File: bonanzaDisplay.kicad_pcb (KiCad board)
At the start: 6 copper layers, 76 x 101 mm, 63 parts, among them J1 OLED-1.31-SSD1322, J15 SWD, J5 Conn_01x10, J6 USB_C_Receptacle_USB2.0, SW1 TS-1088-AR02016, SW2 TS-1088-AR02016, SW4 7*7*5-6P WX, U1 RP2354A, U10 TPS82130, U2 XC6206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

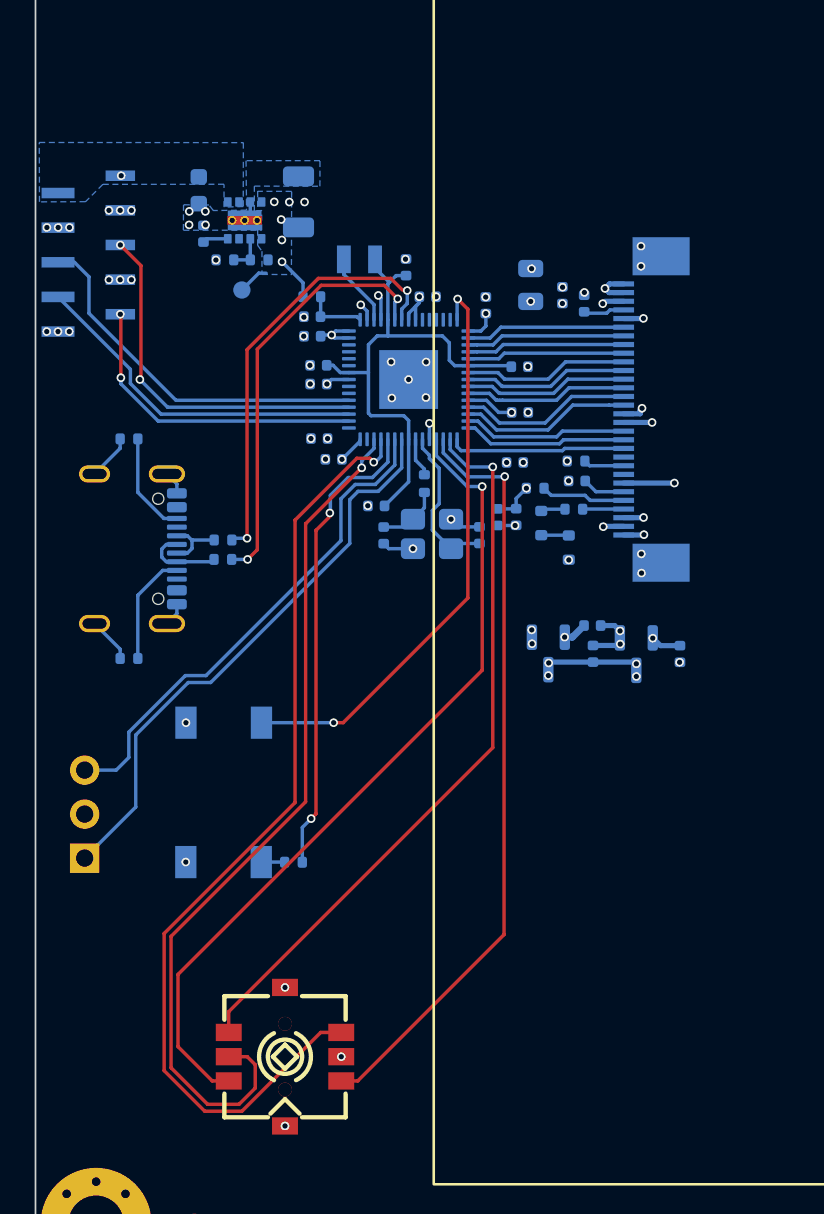
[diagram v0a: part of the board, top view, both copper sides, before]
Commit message: routing cleanup
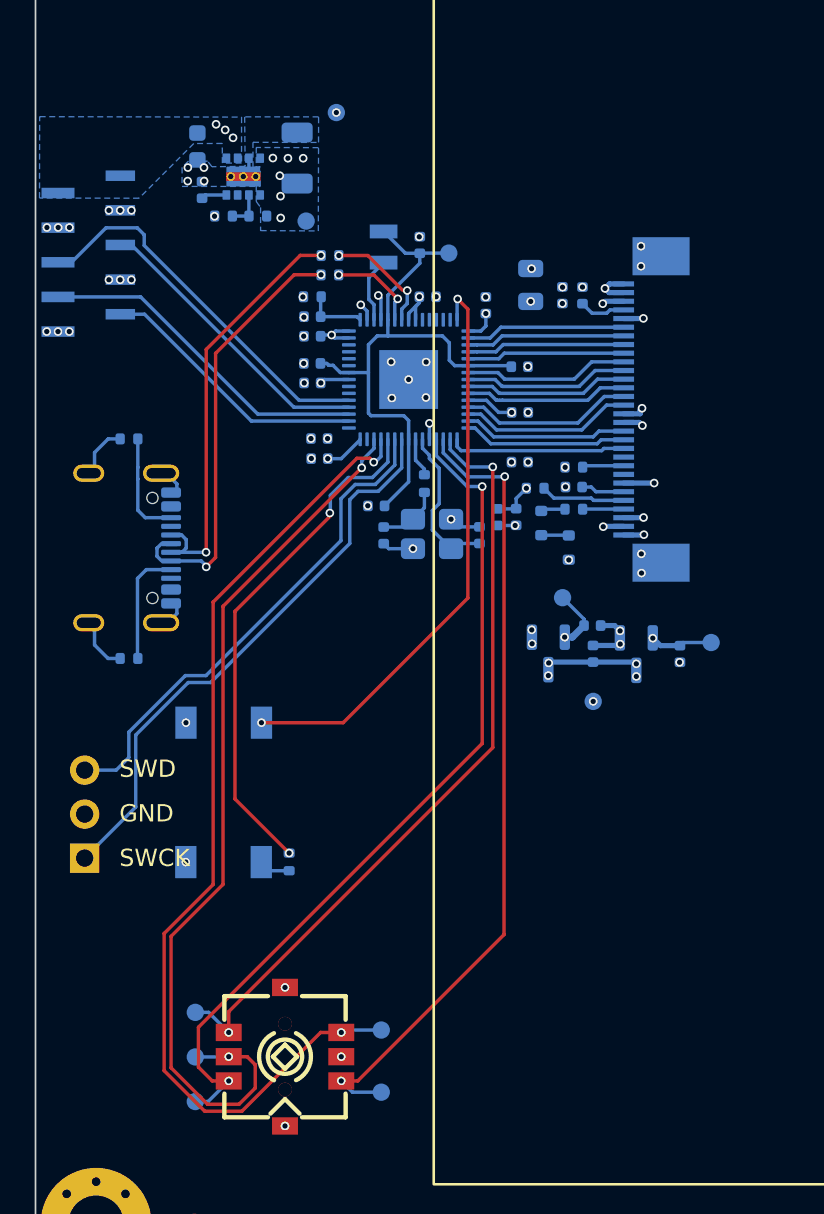
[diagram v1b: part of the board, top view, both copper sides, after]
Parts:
- added TP10: SW_D, bonanzaDisplay:TestPoint_Pad_D1.0mm, B.Cu at (120.0, 125.3)
- added TP11: SW_B, bonanzaDisplay:TestPoint_Pad_D1.0mm, B.Cu at (120.0, 128.9)
- added TP12: SW_A, bonanzaDisplay:TestPoint_Pad_D1.0mm, B.Cu at (109.2, 124.3)
- added TP13: SW_C, bonanzaDisplay:TestPoint_Pad_D1.0mm, B.Cu at (109.2, 129.5)
- added TP14: SW_CEN, bonanzaDisplay:TestPoint_Pad_D1.0mm, B.Cu at (109.2, 126.9)
- added TP15: 3V0, bonanzaDisplay:TestPoint_Pad_D1.0mm, B.Cu at (130.4, 100.4)
- added TP16: 2V8, bonanzaDisplay:TestPoint_Pad_D1.0mm, B.Cu at (139.0, 103.0)
- added TP17: 1V1, bonanzaDisplay:TestPoint_Pad_D1.0mm, B.Cu at (123.9, 80.5)
- added TP18: GND, bonanzaDisplay:TestPoint_Pad_D1.0mm, B.Cu at (132.2, 106.4)
- added TP19: GND, bonanzaDisplay:TestPoint_Pad_D1.0mm, B.Cu at (117.4, 72.4)
- U2: value XC6206 -> XC6206P302MR
- U3: value XC6206 -> XC6206P282MR
- moved R37 17.6 mm to (117.0, 80.6)
- moved R38 17.6 mm to (117.0, 81.7)
- moved TP9 5.44 mm to (115.6, 78.6)
- moved C29 2.53 mm to (109.6, 76.8)
- moved C34 2.53 mm to (115.1, 75.0)
- moved C8 2.53 mm to (109.3, 74.3)
- moved R12 2.53 mm to (112.8, 78.3)
- moved R13 2.53 mm to (110.9, 78.3)
- moved U10 2.53 mm to (112.0, 76.0)
- moved L1 1.57 mm to (120.1, 80.1), turned to -90 degrees
- moved C24 1.52 mm to (122.2, 80.0)
- moved C31 0.82 mm to (116.4, 92.3)
- moved C26 0.48 mm to (131.6, 82.9)
- moved C22 0.39 mm to (131.1, 94.0)
- moved C15 0.38 mm to (116.0, 86.8)
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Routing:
- net /USB_DP: track 3.73 -> 24.5 mm, vias 0 -> 2
- net /USB_DN: track 4.64 -> 24.6 mm, vias 0 -> 2
- net Net-(U1-USB_DM): track 24.5 -> 5.26 mm
- net Net-(U1-USB_DP): track 24.6 -> 6.33 mm
- net /12V: track 47.6 -> 42.0 mm, vias 5 -> 7
- net /1V1: track 30.3 -> 34.6 mm
- net /DISP_GPIO1: track 21.0 -> 17.1 mm, vias 2 -> 0
- net /3V3: track 25.2 -> 22.0 mm, vias 20 -> 21
- net /SW_B: track 44.3 -> 46.9 mm, vias 1 -> 2
- net /SW_A: track 42.4 -> 44.9 mm, vias 1 -> 2
- net Net-(U1-RUN): track 27.3 -> 29.7 mm
- net /SW_D: track 55.7 -> 58.0 mm, vias 1 -> 2
- net /DISP_SDA: track 18.1 -> 15.8 mm, vias 2 -> 0
- net /SW_CEN: track 50.4 -> 52.4 mm, vias 1 -> 2
- net /3V0: track 30.6 -> 32.3 mm
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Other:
- board text added: "BOOT"
- board text added: "GND"
- board text added: "RESET"
- board text added: "SWCK"
- board text added: "SWD"

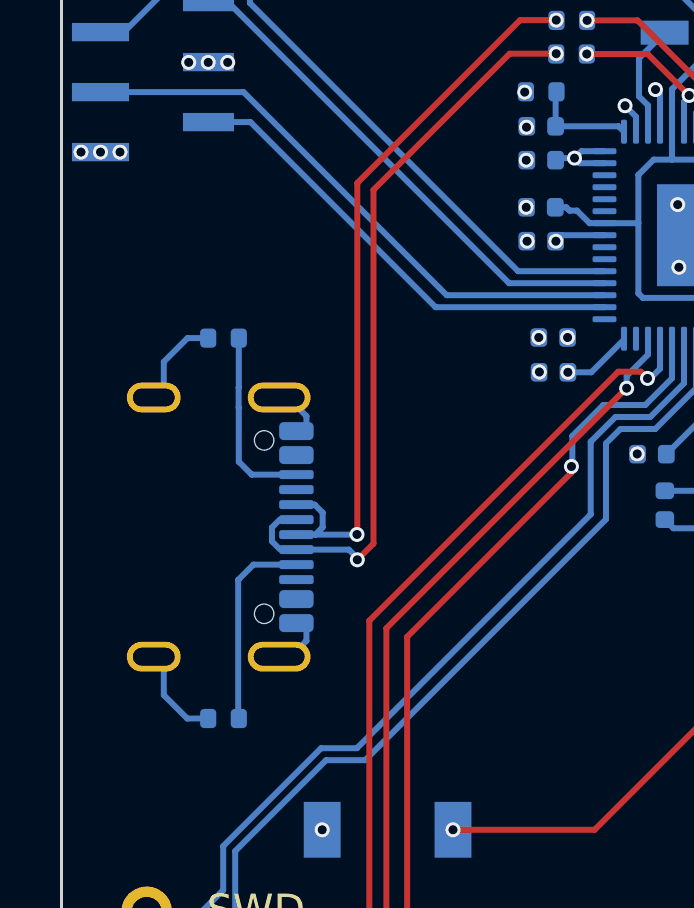
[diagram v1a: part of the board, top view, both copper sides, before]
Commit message: updated RP2354A inductor footprint. fixed USB port position. fixed corrupted footprint library
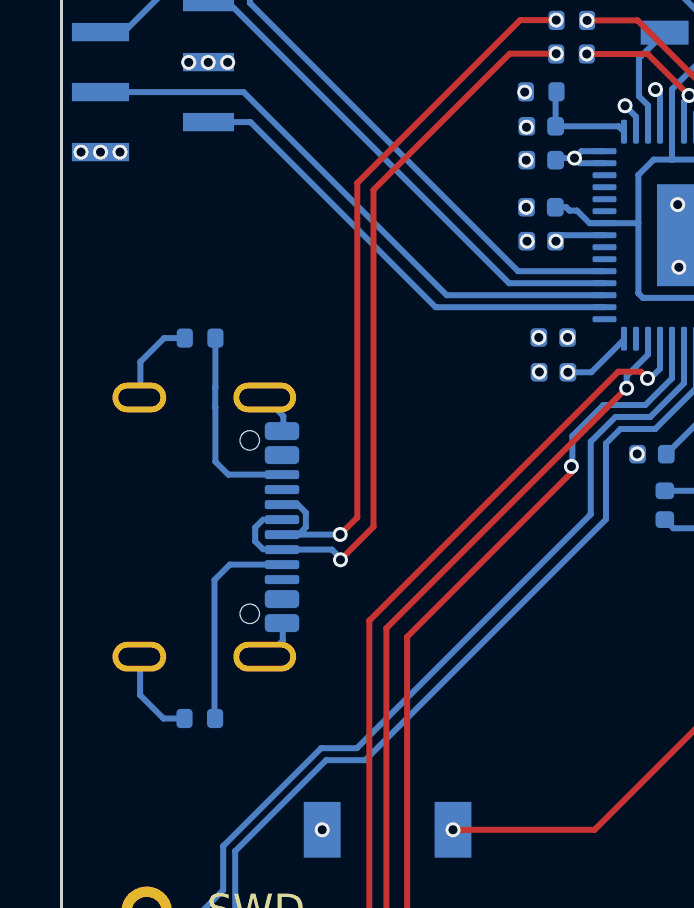
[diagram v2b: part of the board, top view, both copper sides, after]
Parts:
- moved R2 0.79 mm to (104.6, 103.9)
- moved R4 0.78 mm to (104.6, 91.2)
- moved J6 0.48 mm to (103.7, 97.5)

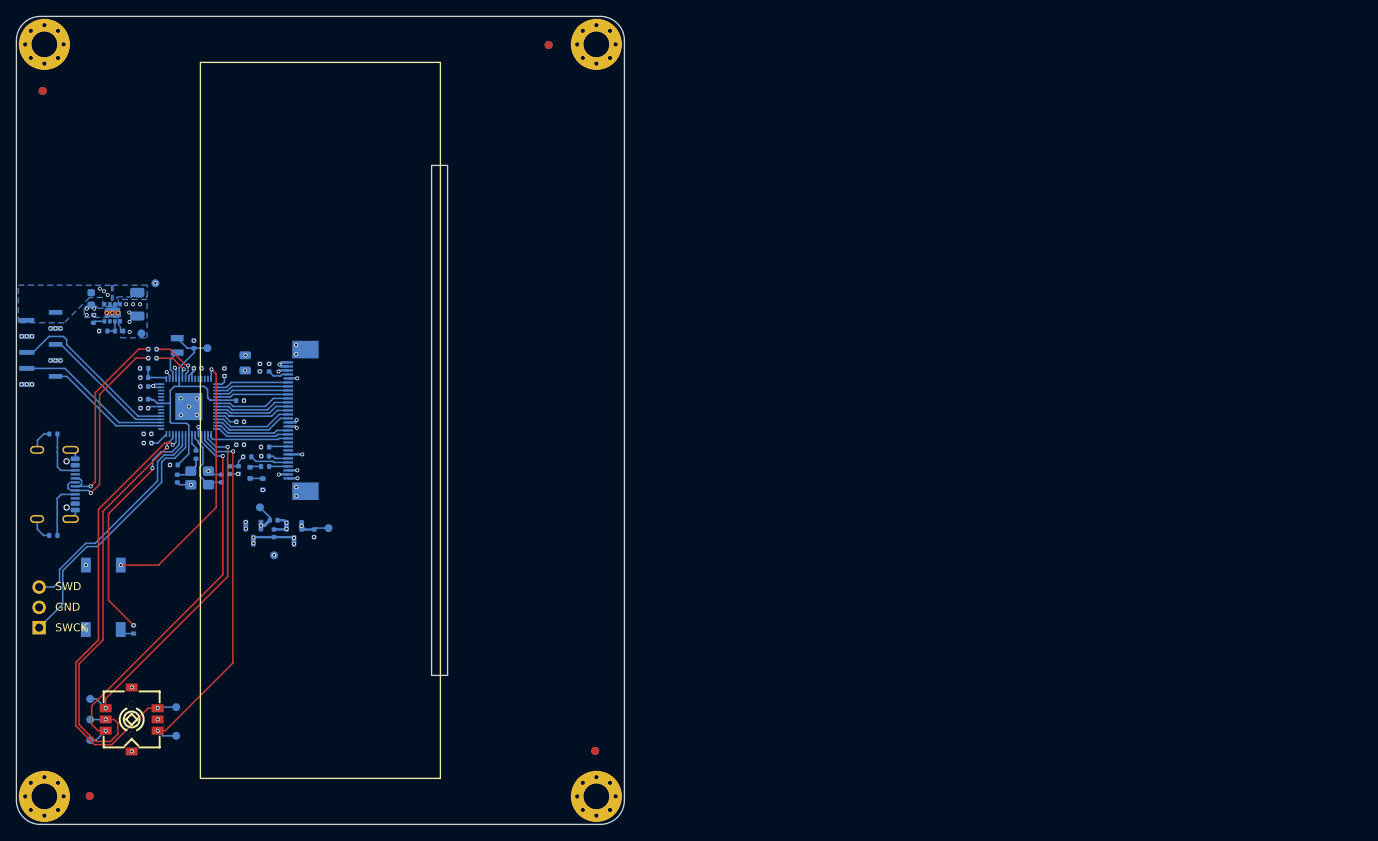
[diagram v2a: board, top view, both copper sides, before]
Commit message: switched to dial switch. added OLED 3D CAD. ordered PCBA
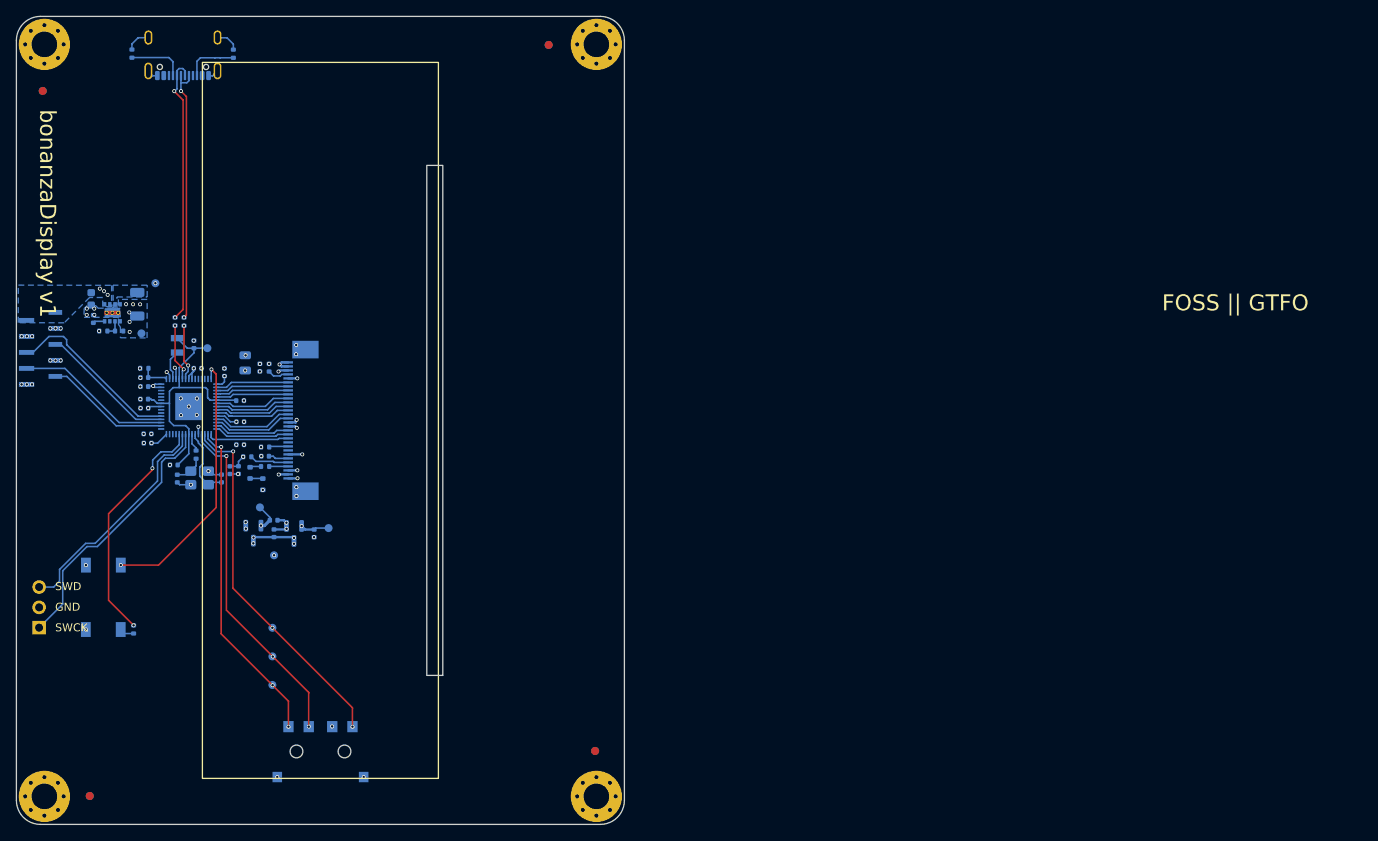
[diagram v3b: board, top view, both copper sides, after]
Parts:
- removed SW4: 7*7*5-6P WX, bonanzaDisplay:SW-SMD_6P-L7.0-W7.0-P1.40-LS7.4-TL
- removed TP10: SW_D, bonanzaDisplay:TestPoint_Pad_D1.0mm
- removed TP11: SW_B, bonanzaDisplay:TestPoint_Pad_D1.0mm
- added SW3: SIQ-02FVS3_C41430892, bonanzaDisplay:SW-SMD_SIQ-02FVS3, B.Cu at (138.0, 130.9)
- TP12: value SW_A -> SW_CCW
- TP13: value SW_C -> SW_SW
- TP14: value SW_CEN -> SW_CW
- moved R2 61.0 mm to (114.4, 43.7), turned to -90 degrees
- moved J6 57.4 mm to (120.8, 42.7), turned to 0 degrees
- moved R4 52.6 mm to (127.1, 43.7), turned to -90 degrees
- moved TP14 25.5 mm to (132.0, 115.4), turned to 180 degrees
- moved TP13 25.1 mm to (132.0, 119.0), turned to 180 degrees
- moved TP12 22.8 mm to (132.0, 122.6)
- moved R38 5.39 mm to (119.8, 77.1), turned to -90 degrees
- moved R37 5.24 mm to (121.0, 77.2), turned to -90 degrees
- moved J5 4.88 mm to (103.0, 80.5)
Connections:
- net /SW_A renamed /SW_CCW
- net /SW_C renamed /SW_SW
- TP14 pad 1: /SW_CEN -> /SW_CW
- U1 pad 18: /SW_B -> /SW_CW
- U1 pad 27: /SW_D -> unconnected-(U1-GPIO16-Pad27)
- U1 pad 28: /SW_CEN -> unconnected-(U1-GPIO17-Pad28)
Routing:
- net /SW_D: track 58.0 -> 0.00 mm, vias 2 -> 0
- net /SW_CEN: track 52.4 -> 0.00 mm, vias 2 -> 0
- net /SW_B: track 46.9 -> 0.00 mm, vias 2 -> 0
- net /SW_CW: track 0.00 -> 45.6 mm, vias 0 -> 3
- net /USB_DN: track 24.2 -> 33.8 mm
- net /USB_DP: track 24.8 -> 32.6 mm
- net /SW_SW: track 49.2 -> 42.9 mm, vias 2 -> 3
- net /SW_CCW: track 44.9 -> 41.1 mm, vias 2 -> 3
- net Net-(U1-USB_DM): track 5.26 -> 7.19 mm
- net Net-(U1-USB_DP): track 6.33 -> 7.01 mm
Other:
- board text added: "FOSS || GTFO"
- board text added: "bonanzaDisplay v1"

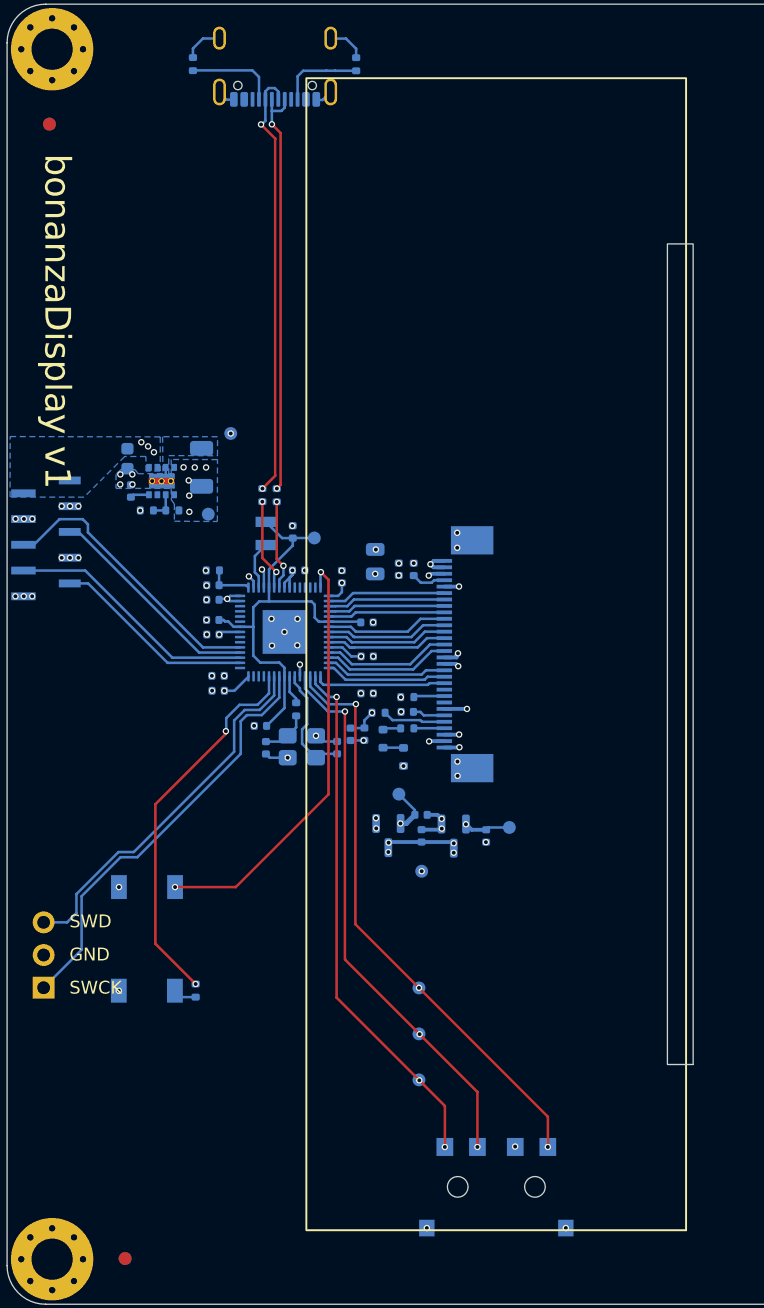
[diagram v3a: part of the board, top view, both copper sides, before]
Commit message: fix display connector pinout for #1
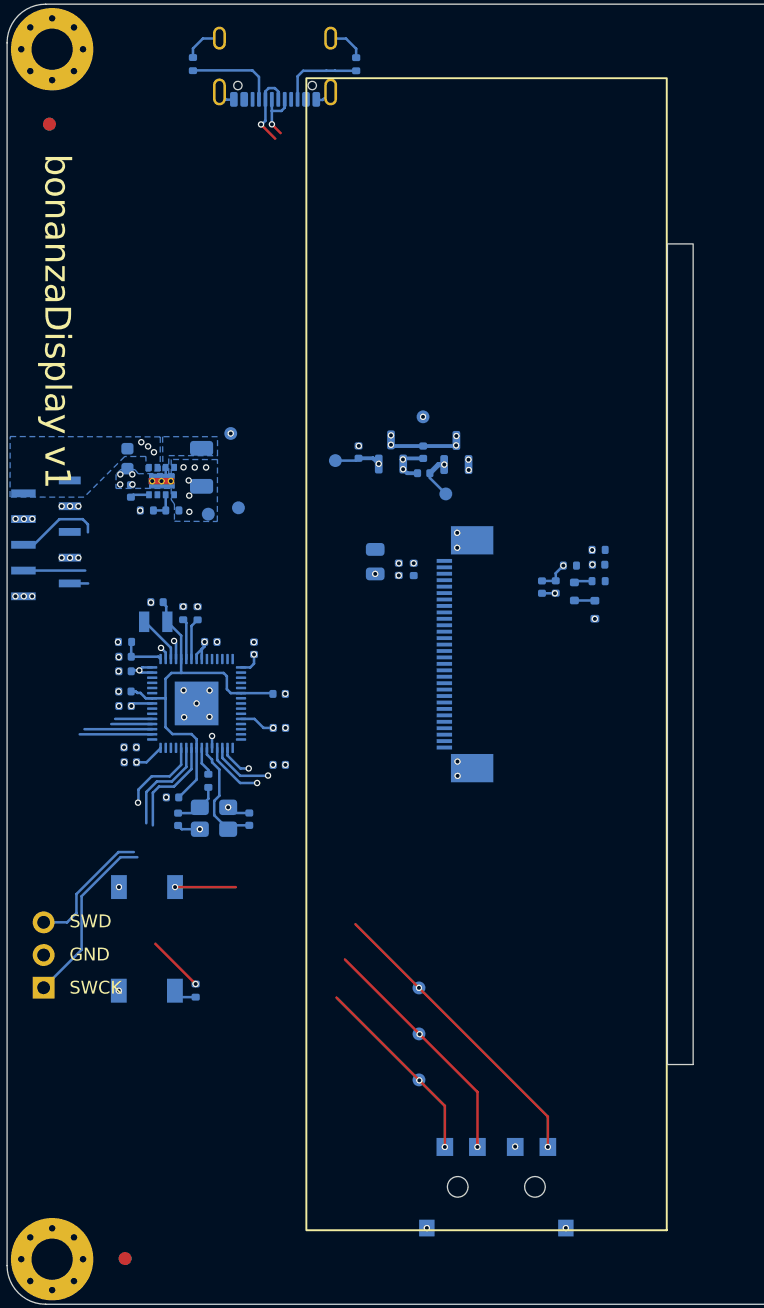
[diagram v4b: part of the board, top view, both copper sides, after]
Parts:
- moved TP18 35.3 mm to (132.3, 71.1), turned to 180 degrees
- moved TP16 31.5 mm to (125.5, 74.5), turned to 180 degrees
- moved C40 31.4 mm to (127.3, 73.8), turned to 90 degrees
- moved U3 30.2 mm to (129.8, 73.8), turned to 90 degrees
- moved U2 30.2 mm to (134.9, 73.8), turned to 90 degrees
- moved C39 29.8 mm to (132.3, 73.8), turned to -90 degrees
- moved C38 26.5 mm to (132.4, 75.4), turned to 180 degrees
- moved TP15 23.6 mm to (134.1, 77.0), turned to 180 degrees
- moved C21 18.8 mm to (141.6, 84.3)
- moved C22 18.8 mm to (146.0, 82.5)
- moved R34 18.8 mm to (146.0, 83.8)
- moved R35 18.8 mm to (146.0, 81.4)
- moved C19 18.8 mm to (142.6, 84.3)
- moved D2 18.8 mm to (145.7, 86.0)
- moved D3 18.8 mm to (144.1, 84.6)
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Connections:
- U1 pad 10: /D0 -> /D7
- U1 pad 12: /E/RD -> /RES
- U1 pad 13: /R/W -> /CS
- U1 pad 15: /CS -> /R/W
- U1 pad 16: /RES -> /E/RD
- U1 pad 2: /D7 -> /D0
- U1 pad 3: /D6 -> /D1
- U1 pad 4: /D5 -> /D2
- U1 pad 5: /D4 -> /D3
- U1 pad 7: /D3 -> /D4
- U1 pad 8: /D2 -> /D5
- U1 pad 9: /D1 -> /D6
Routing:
- net Net-(U1-~{QSPI_SS}): track 33.6 -> 4.72 mm, vias 2 -> 1
- net /USB_DP: track 32.6 -> 4.91 mm
- net /USB_DN: track 33.8 -> 6.21 mm
- net /3V0: track 32.3 -> 6.03 mm, vias 3 -> 2
- net /SW_CCW: track 41.1 -> 17.7 mm
- net /SW_SW: track 42.9 -> 23.6 mm
- net Net-(U1-RUN): track 29.7 -> 10.9 mm
- net /SW_CW: track 45.6 -> 28.4 mm
- net /DISP_GPIO1: track 17.1 -> 3.83 mm
- net /DISP_GPIO2: track 22.1 -> 9.47 mm
- net /2V8: track 15.4 -> 3.65 mm, vias 2 -> 1
- net /SWCLK: track 33.2 -> 21.9 mm
- net /SWD: track 29.0 -> 17.9 mm
- net /RES: track 10.2 -> 0.00 mm
- net /E/RD: track 9.98 -> 0.00 mm
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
